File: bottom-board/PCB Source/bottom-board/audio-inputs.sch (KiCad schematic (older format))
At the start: 81 parts, among them P10 JACK_TRS_6PINS, P9 JACK_TRS_6PINS, Q1 2N7002, Q2 2N7002, Q3 MMBFJ110, Q4 MMBFJ110, Q5 MMBFJ110, Q6 MMBFJ110, Q7 2N7002, Q8 2N7002, U5 LM4562

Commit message: update fabrication data
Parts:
- C37: footprint Capacitor_SMD:C_0603_1608Metric -> Capacitor_SMD:C_0805_2012Metric; MPN EMK107BBJ106MA-T -> GRM219R61E106KA12D
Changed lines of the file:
@@
 F 0 "C37" H 9330 5315 50  0000 R CNN
 F 1 "10uF" H 9160 5225 50  0000 L CNN
-F 2 "Capacitor_SMD:C_0603_1608Metric" H 9430 5295 60  0001 C CNN
+F 2 "Capacitor_SMD:C_0805_2012Metric" H 9430 5295 60  0001 C CNN
 F 3 "" H 9430 5295 60  0000 C CNN
-F 4 "EMK107BBJ106MA-T" H 4980 3595 50  0001 C CNN "MPN"
+F 4 "GRM219R61E106KA12D" H 4980 3595 50  0001 C CNN "MPN"
 	1    9430 5295
 	-1   0    0    1

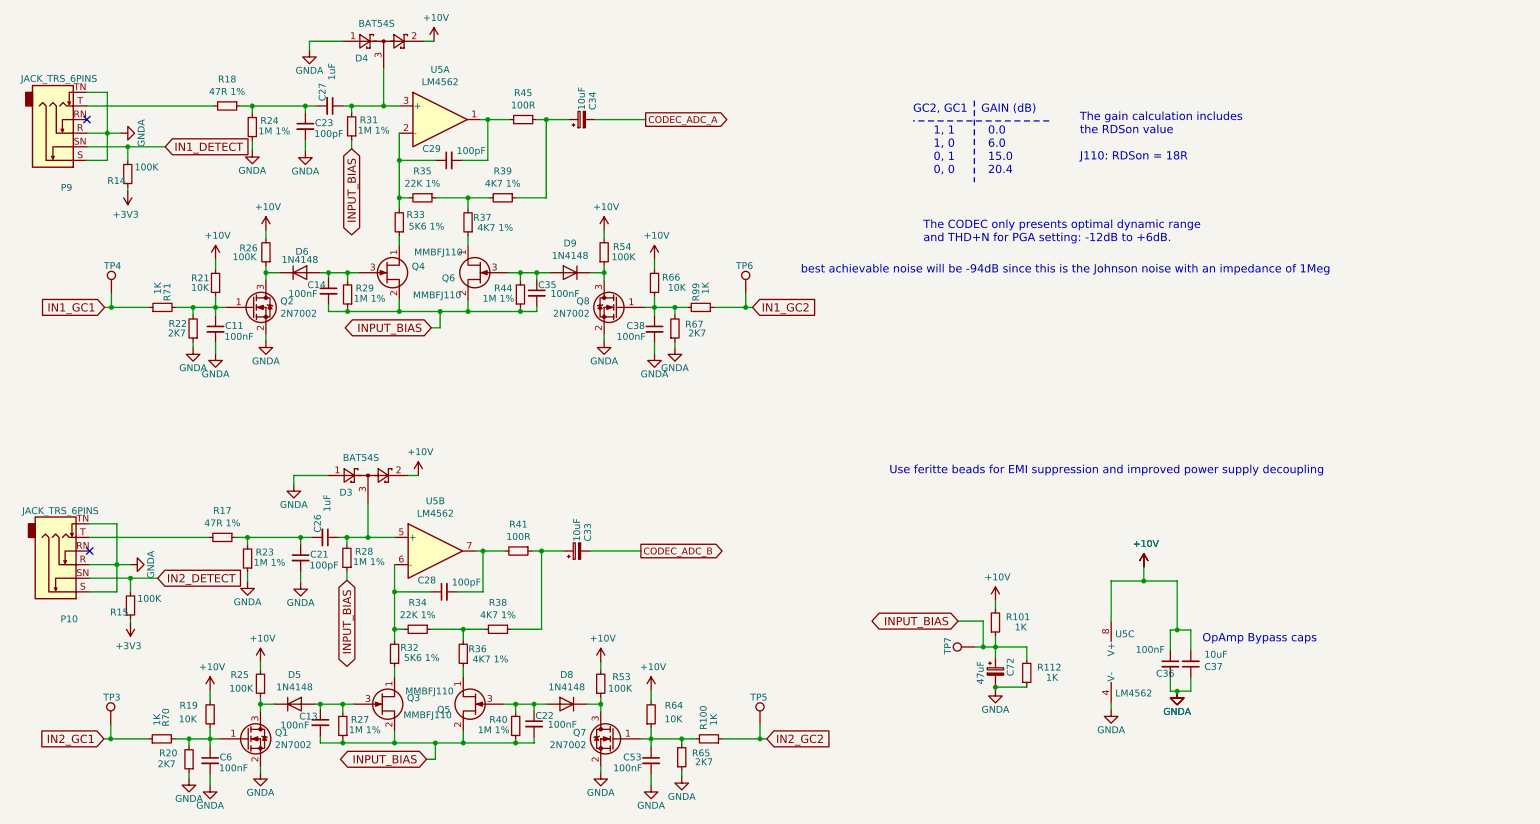
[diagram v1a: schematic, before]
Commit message: change input bias 5->6V, reduce harmonics
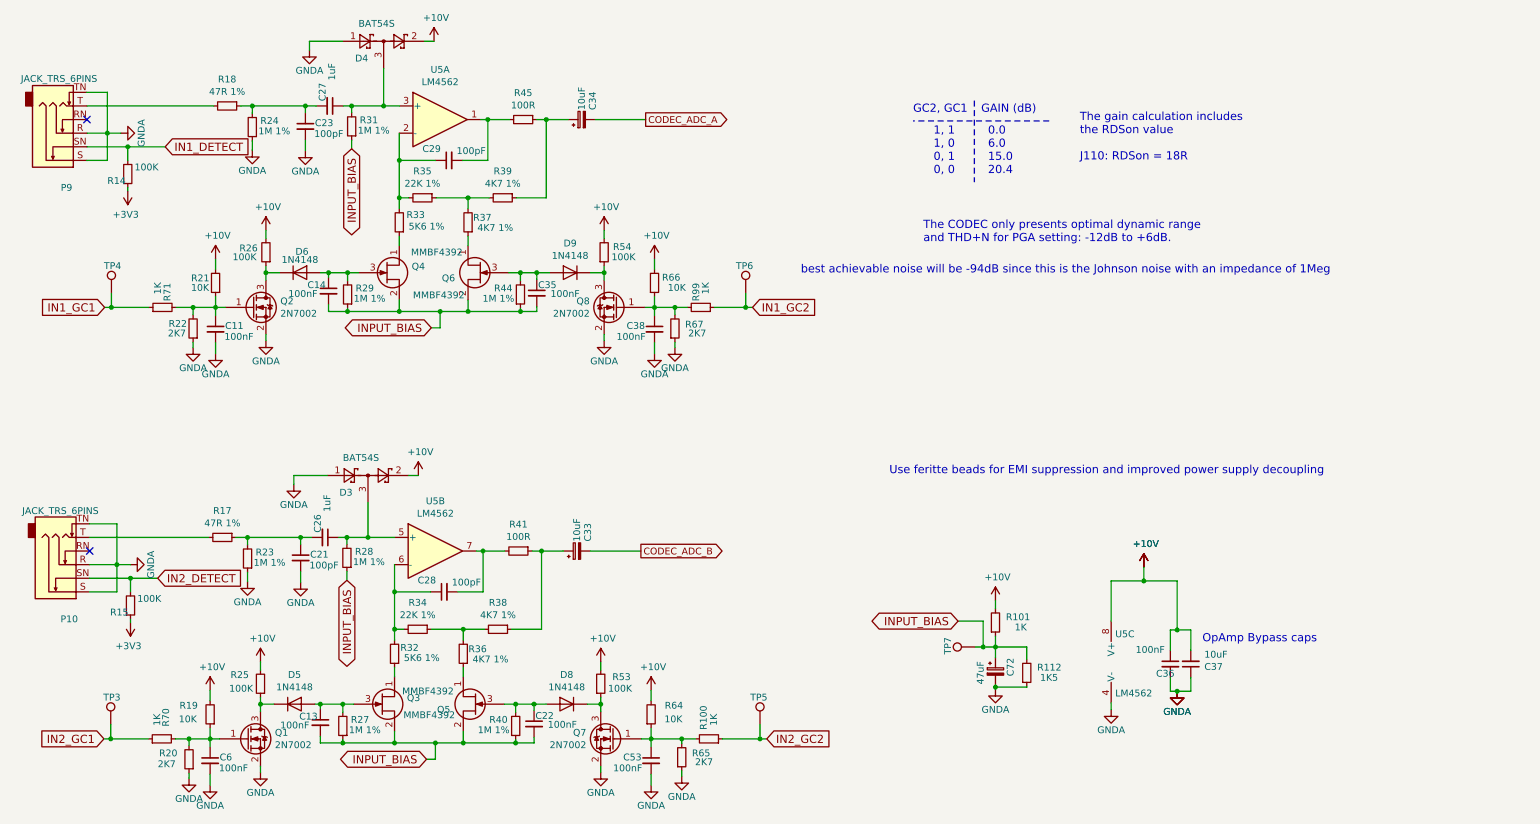
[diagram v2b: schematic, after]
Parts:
- Q3, Q4, Q5, Q6: value MMBFJ110 -> MMBF4392; MPN MMBFJ110 -> MMBF4392LT1G
- R101: MPN ERJ-PB3D1501V -> ERJ-PB3D1001V
- R112: value 1K -> 1K5; MPN ERJ-PB3D1001V -> (none)
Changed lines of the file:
@@
 P 3515 2420
 F 0 "Q4" H 3706 2466 50  0000 L CNN
-F 1 "MMBFJ110" H 3715 2255 50  0000 L CNN
+F 1 "MMBF4392" H 3715 2255 50  0000 L CNN
 F 2 "Package_TO_SOT_SMD:SOT-23" H 3715 2520 50  0001 C CNN
 F 3 "" H 3515 2420 50  0001 C CNN
-F 4 "MMBFJ110" H 3515 2420 50  0001 C CNN "MPN"
+F 4 "MMBF4392LT1G" H 3515 2420 50  0001 C CNN "MPN"
 	1    3515 2420
 	1    0    0    -1
@@
 P 4220 2420
 F 0 "Q6" H 4415 2380 50  0000 L CNN
-F 1 "MMBFJ110" H 4360 2570 50  0000 L CNN
+F 1 "MMBF4392" H 4360 2570 50  0000 L CNN
 F 2 "Package_TO_SOT_SMD:SOT-23" H 4420 2520 50  0001 C CNN
 F 3 "" H 4220 2420 50  0001 C CNN
-F 4 "MMBFJ110" H 4220 2420 50  0001 C CNN "MPN"
+F 4 "MMBF4392LT1G" H 4220 2420 50  0001 C CNN "MPN"
 	1    4220 2420
 	-1   0    0    -1
@@
 P 3480 5590
 F 0 "Q3" H 3671 5636 50  0000 L CNN
-F 1 "MMBFJ110" H 3645 5510 50  0000 L CNN
+F 1 "MMBF4392" H 3645 5510 50  0000 L CNN
 F 2 "Package_TO_SOT_SMD:SOT-23" H 3680 5690 50  0001 C CNN
 F 3 "" H 3480 5590 50  0001 C CNN
-F 4 "MMBFJ110" H 3480 5590 50  0001 C CNN "MPN"
+F 4 "MMBF4392LT1G" H 3480 5590 50  0001 C CNN "MPN"
 	1    3480 5590
 	1    0    0    -1
@@
 P 4185 5590
 F 0 "Q5" H 4380 5550 50  0000 L CNN
-F 1 "MMBFJ110" H 4355 5685 50  0000 L CNN
+F 1 "MMBF4392" H 4355 5685 50  0000 L CNN
 F 2 "Package_TO_SOT_SMD:SOT-23" H 4385 5690 50  0001 C CNN
 F 3 "" H 4185 5590 50  0001 C CNN
-F 4 "MMBFJ110" H 4185 5590 50  0001 C CNN "MPN"
+F 4 "MMBF4392LT1G" H 4185 5590 50  0001 C CNN "MPN"
 	1    4185 5590
 	-1   0    0    -1
@@
 F 2 "Resistor_SMD:R_0603_1608Metric" H 7995 4990 50  0001 C CNN
 F 3 "~" H 7995 4990 50  0001 C CNN
-F 4 "ERJ-PB3D1501V" V 7995 4990 50  0001 C CNN "MPN"
+F 4 "ERJ-PB3D1001V" V 7995 4990 50  0001 C CNN "MPN"
 	1    7995 4990
 	1    0    0    1
@@
 P 8225 5360
 F 0 "R112" H 8480 5320 50  0000 R CNN
-F 1 "1K" H 8455 5395 50  0000 R CNN
+F 1 "1K5" H 8455 5395 50  0000 R CNN
 F 2 "Resistor_SMD:R_0603_1608Metric" H 8225 5360 50  0001 C CNN
 F 3 "~" H 8225 5360 50  0001 C CNN
-F 4 "ERJ-PB3D1001V" V 8225 5360 50  0001 C CNN "MPN"
 	1    8225 5360
 	1    0    0    1

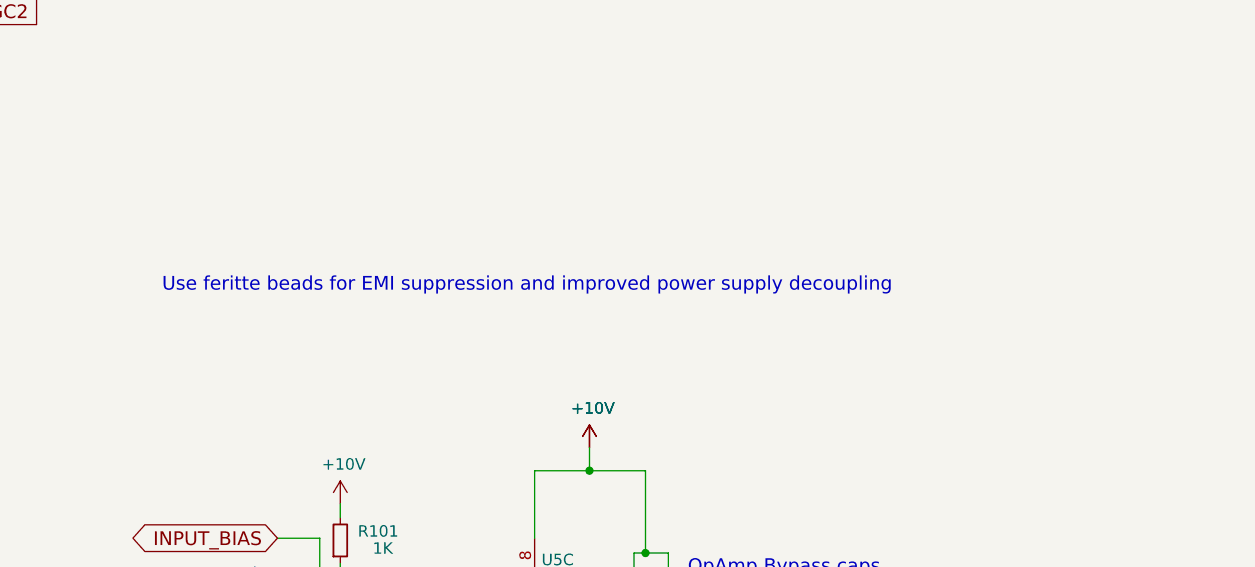
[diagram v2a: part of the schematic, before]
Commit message: change MPN of U10 and U12
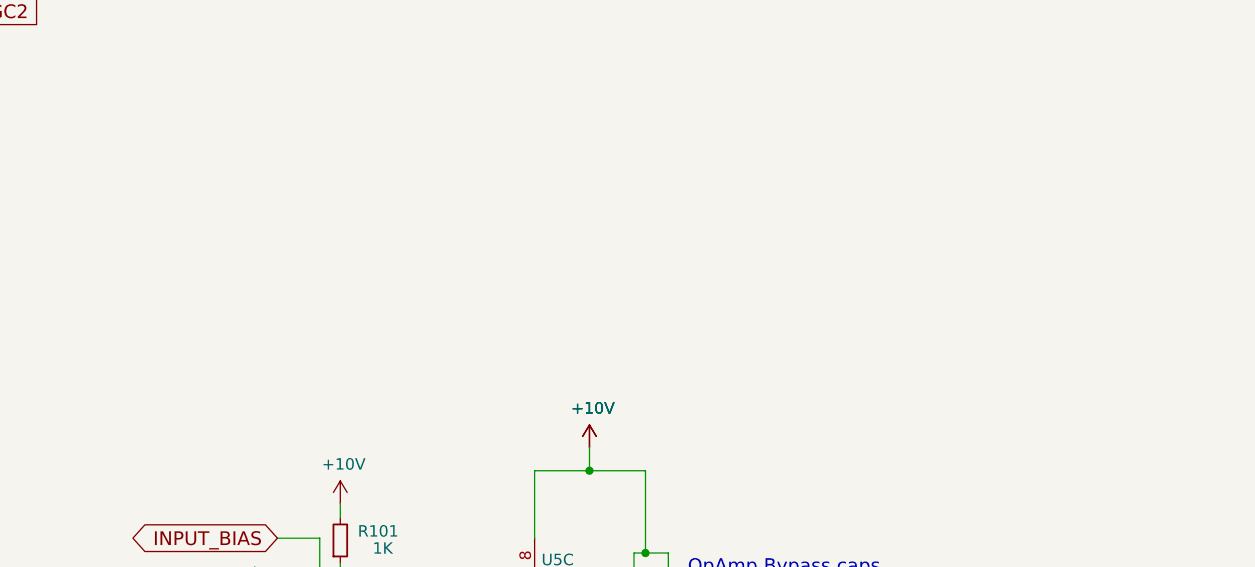
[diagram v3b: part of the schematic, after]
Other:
- note removed: "Use feritte beads for EMI suppression and improved power supply decoupling"
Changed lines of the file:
@@
 Wire Wire Line
 	2925 1445 2925 1525
-$Comp
-L bottom-board-rescue:C_Small C?
-U 1 1 5F1286D8
-P 3105 1195
-AR Path="/54F72B97/5F1286D8" Ref="C?"  Part="1"
-AR Path="/54F72C8D/5F1286D8" Ref="C27"  Part="1"
-F 0 "C27" H 2935 1140 50  0000 L CNN
-F 1 "1uF" H 2790 1210 50  0000 L CNN
-F 2 "Capacitor_SMD:C_0603_1608Metric" H 3105 1195 60  0001 C CNN
-F 3 "" H 3105 1195 60  0000 C CNN
-F 4 "TMK107B7105KA-T" H -2195 -4155 50  0001 C CNN "MPN"
-	1    3105 1195
-	0    1    1    0
-$EndComp
 Wire Wire Line
 	3005 1195 2925 1195
@@
 Wire Wire Line
 	8845 5630 8845 5580
-Text Notes 7215 3910 0    60   ~ 0
-Use feritte beads for EMI suppression and improved power supply decoupling
 Text Notes 9515 5145 0    60   ~ 0
 OpAmp Bypass caps
@@
 Wire Wire Line
 	7905 5170 7995 5170
+$Comp
+L bottom-board-rescue:C_Small C?
+U 1 1 5F1286D8
+P 3105 1195
+AR Path="/54F72B97/5F1286D8" Ref="C?"  Part="1"
+AR Path="/54F72C8D/5F1286D8" Ref="C27"  Part="1"
+F 0 "C27" H 2935 1140 50  0000 L CNN
+F 1 "1uF" H 2790 1210 50  0000 L CNN
+F 2 "Capacitor_SMD:C_0603_1608Metric" H 3105 1195 60  0001 C CNN
+F 3 "" H 3105 1195 60  0000 C CNN
+F 4 "TMK107B7105KA-T" H -2195 -4155 50  0001 C CNN "MPN"
+	1    3105 1195
+	0    1    1    0
+$EndComp
 $EndSCHEMATC

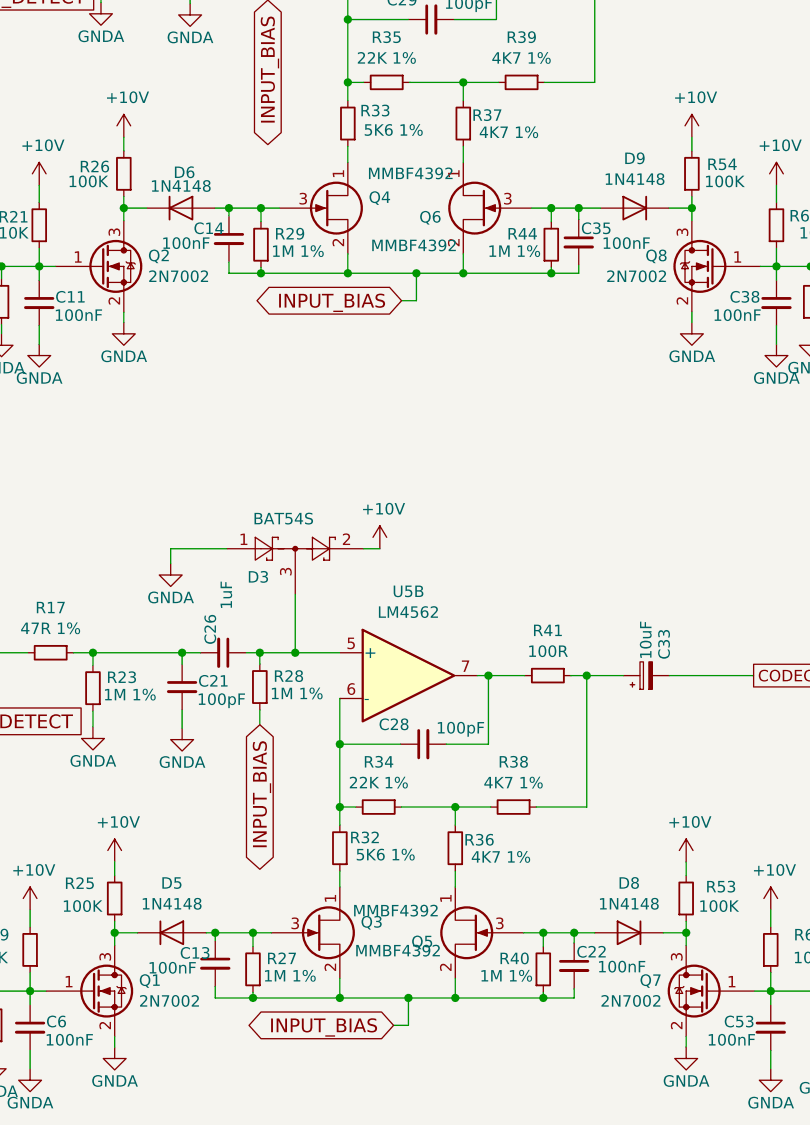
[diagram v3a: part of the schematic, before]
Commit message: change JFET MPN
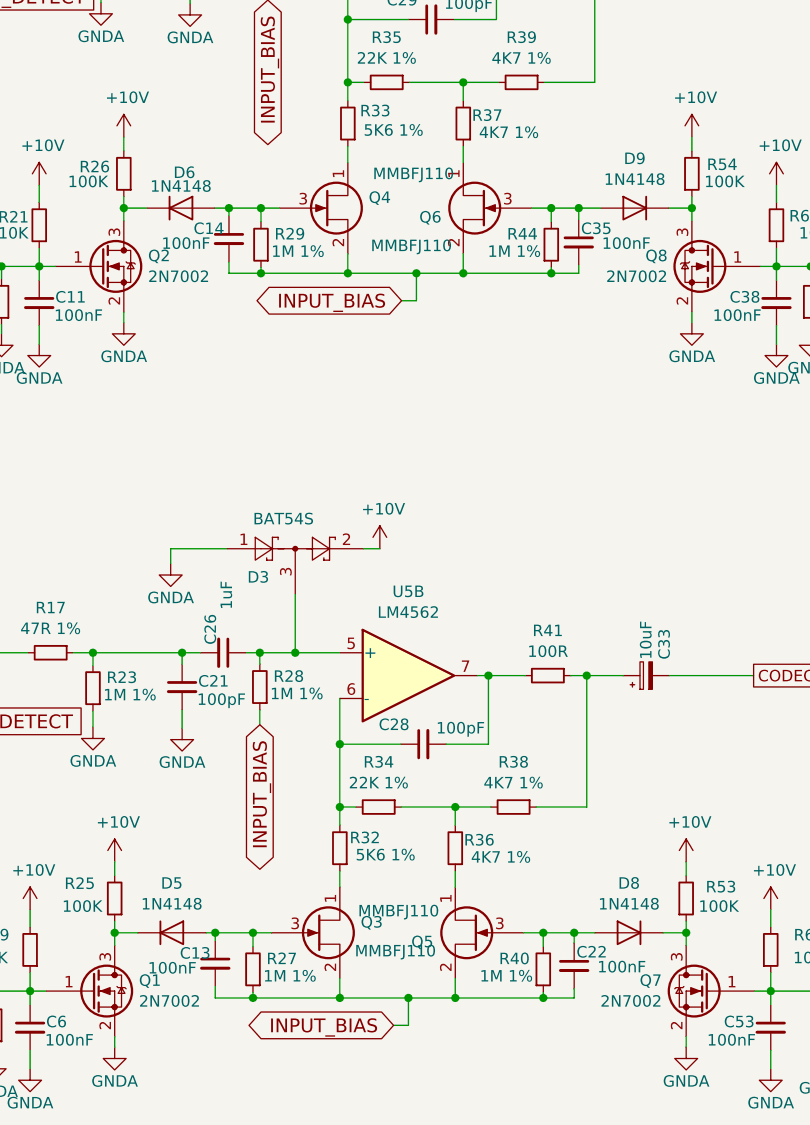
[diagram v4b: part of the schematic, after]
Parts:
- Q3, Q4, Q5, Q6: value MMBF4392 -> MMBFJ110; MPN MMBF4392LT1G -> MMBFJ110
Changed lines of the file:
@@
 P 3515 2420
 F 0 "Q4" H 3706 2466 50  0000 L CNN
-F 1 "MMBF4392" H 3715 2255 50  0000 L CNN
+F 1 "MMBFJ110" H 3715 2255 50  0000 L CNN
 F 2 "Package_TO_SOT_SMD:SOT-23" H 3715 2520 50  0001 C CNN
 F 3 "" H 3515 2420 50  0001 C CNN
-F 4 "MMBF4392LT1G" H 3515 2420 50  0001 C CNN "MPN"
+F 4 "MMBFJ110" H 3515 2420 50  0001 C CNN "MPN"
 	1    3515 2420
 	1    0    0    -1
@@
 P 4220 2420
 F 0 "Q6" H 4415 2380 50  0000 L CNN
-F 1 "MMBF4392" H 4360 2570 50  0000 L CNN
+F 1 "MMBFJ110" H 4360 2570 50  0000 L CNN
 F 2 "Package_TO_SOT_SMD:SOT-23" H 4420 2520 50  0001 C CNN
 F 3 "" H 4220 2420 50  0001 C CNN
-F 4 "MMBF4392LT1G" H 4220 2420 50  0001 C CNN "MPN"
+F 4 "MMBFJ110" H 4220 2420 50  0001 C CNN "MPN"
 	1    4220 2420
 	-1   0    0    -1
@@
 P 3480 5590
 F 0 "Q3" H 3671 5636 50  0000 L CNN
-F 1 "MMBF4392" H 3645 5510 50  0000 L CNN
+F 1 "MMBFJ110" H 3645 5510 50  0000 L CNN
 F 2 "Package_TO_SOT_SMD:SOT-23" H 3680 5690 50  0001 C CNN
 F 3 "" H 3480 5590 50  0001 C CNN
-F 4 "MMBF4392LT1G" H 3480 5590 50  0001 C CNN "MPN"
+F 4 "MMBFJ110" H 3480 5590 50  0001 C CNN "MPN"
 	1    3480 5590
 	1    0    0    -1
@@
 P 4185 5590
 F 0 "Q5" H 4380 5550 50  0000 L CNN
-F 1 "MMBF4392" H 4355 5685 50  0000 L CNN
+F 1 "MMBFJ110" H 4355 5685 50  0000 L CNN
 F 2 "Package_TO_SOT_SMD:SOT-23" H 4385 5690 50  0001 C CNN
 F 3 "" H 4185 5590 50  0001 C CNN
-F 4 "MMBF4392LT1G" H 4185 5590 50  0001 C CNN "MPN"
+F 4 "MMBFJ110" H 4185 5590 50  0001 C CNN "MPN"
 	1    4185 5590
 	-1   0    0    -1
